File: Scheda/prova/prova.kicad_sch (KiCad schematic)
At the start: 26 parts, among them J2 Conn_01x02, J3 Conn_01x02, J4 Signal_Out, J5 Signal_Out, J6 Supply, J7 Test, J8 Test, J9 Vbias, U1 Opamp_Quad

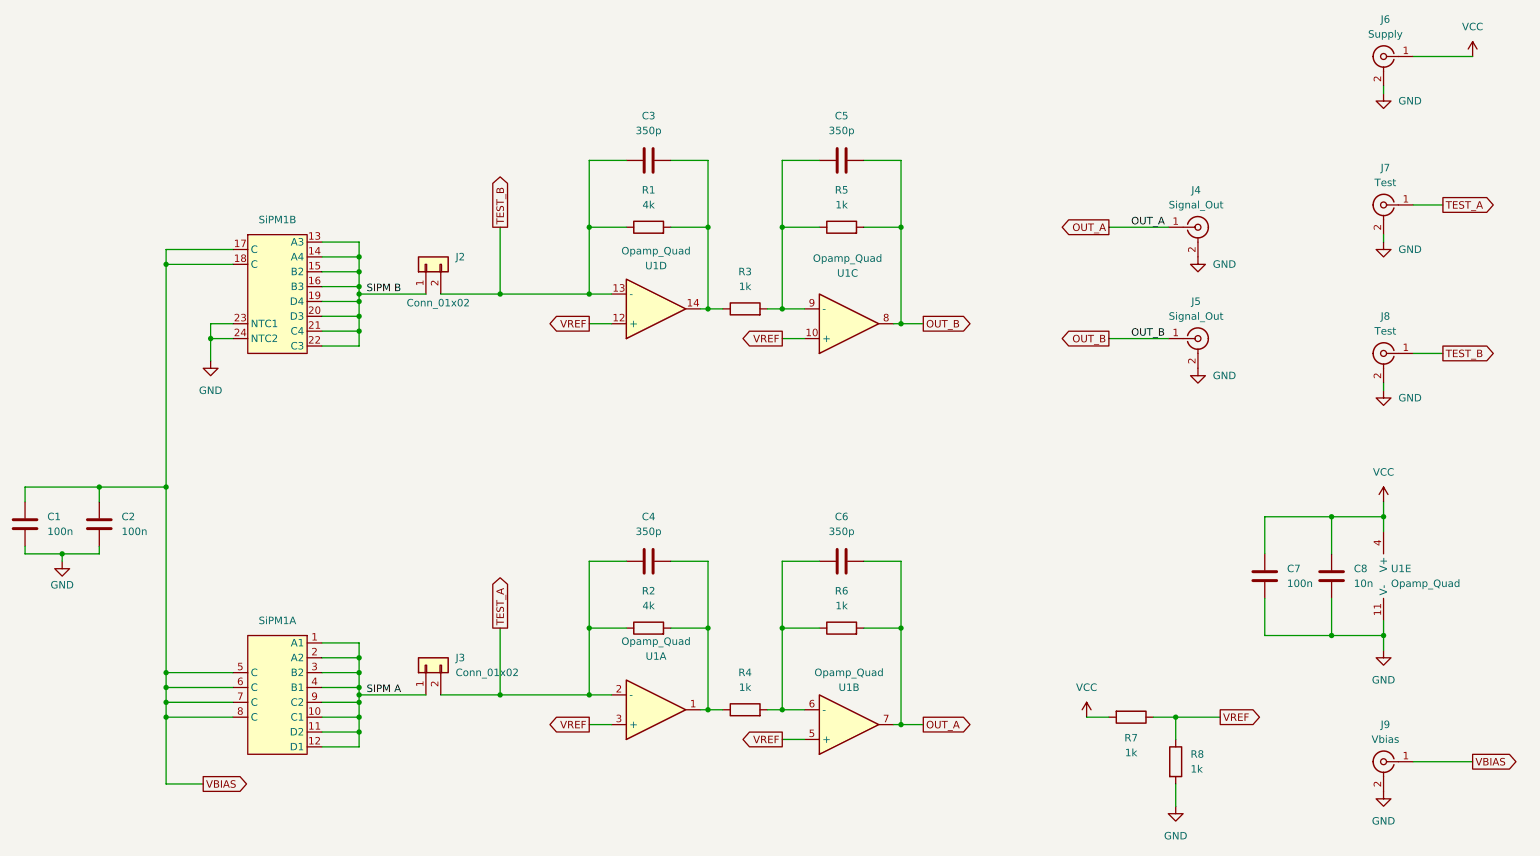
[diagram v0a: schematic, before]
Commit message: Aggiunta modelli 3D e regolatore
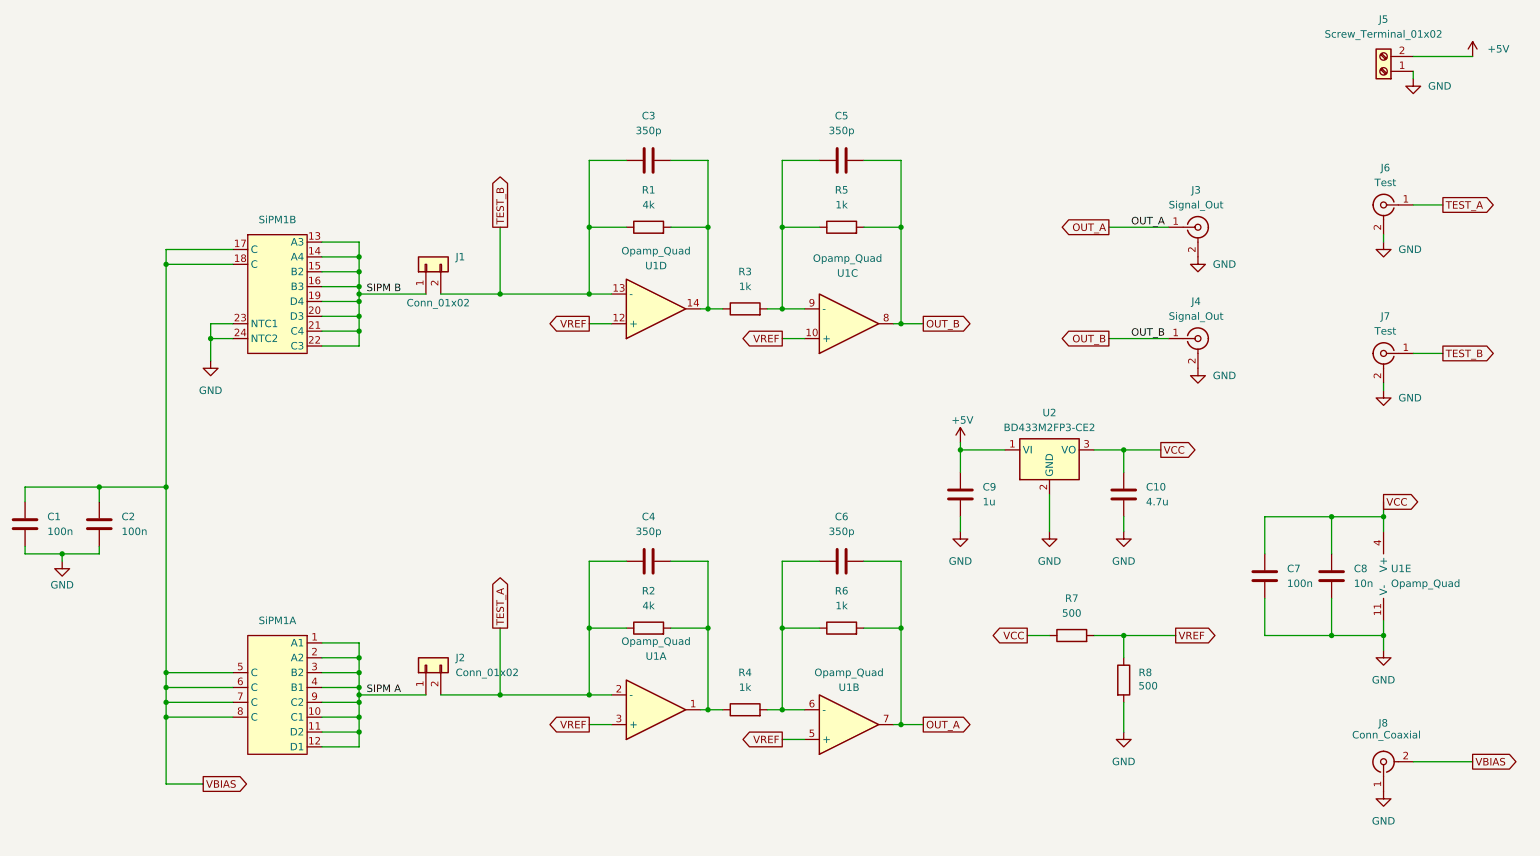
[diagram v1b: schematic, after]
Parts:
- removed J6: Supply, SPaRKLE-Footprints:SMA_Horizontal, symbol Connector:Conn_Coaxial
- removed J9: Vbias, SPaRKLE-Footprints:SMA_Horizontal, symbol Connector:Conn_Coaxial
- added C10: 4.7u, Capacitor_SMD:C_0603_1608Metric_Pad1.08x0.95mm_HandSolder, symbol Device:C
- added C9: 1u, Capacitor_SMD:C_0603_1608Metric_Pad1.08x0.95mm_HandSolder, symbol Device:C
- added J5: Screw_Terminal_01x02, SPaRKLE-Footprints:TerminalBlock_Altech_AK300-2_P5.00mm, symbol Connector:Screw_Terminal_01x02
- added J8: Conn_Coaxial, Connector_Coaxial:BNC_Amphenol_B6252HB-NPP3G-50_Horizontal, symbol Connector:Conn_Coaxial
- added U2: BD433M2FP3-CE2, Package_TO_SOT_SMD:SOT-223-3_TabPin2, symbol Regulator_Linear:AMS1117-3.3
- R7, R8: value 1k -> 500
- renumbered J2 to J1, J3 to J2, J4 to J3, J5 to J4, J7 to J6, J8 to J7
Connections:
- net GND: now also C10.2, C9.2, J5.1 (Pin_1), J8.1 (In), U2.2 (GND)
- net VBIAS: now also J8.2 (Ext)
- net VCC: now also R7.1, C10.1, U2.3 (VO); no longer R7.2
- net VREF: now also R7.2; no longer R7.1
- new net +5V: C9.1, J5.2 (Pin_2), U2.1 (VI)
